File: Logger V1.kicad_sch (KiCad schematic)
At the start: 34 parts, among them J1 USB_C_Receptacle_USB2.0_16P, Q1 SS8050, Q2 SS8050, Q3 IRLML6402, SW1 B3U-1000P-B, SW2 B3U-1000P-B, U1 ESP32-WROOM-32E, U2 TLV76733DRVx, U3 LOG Interface, U4 oled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

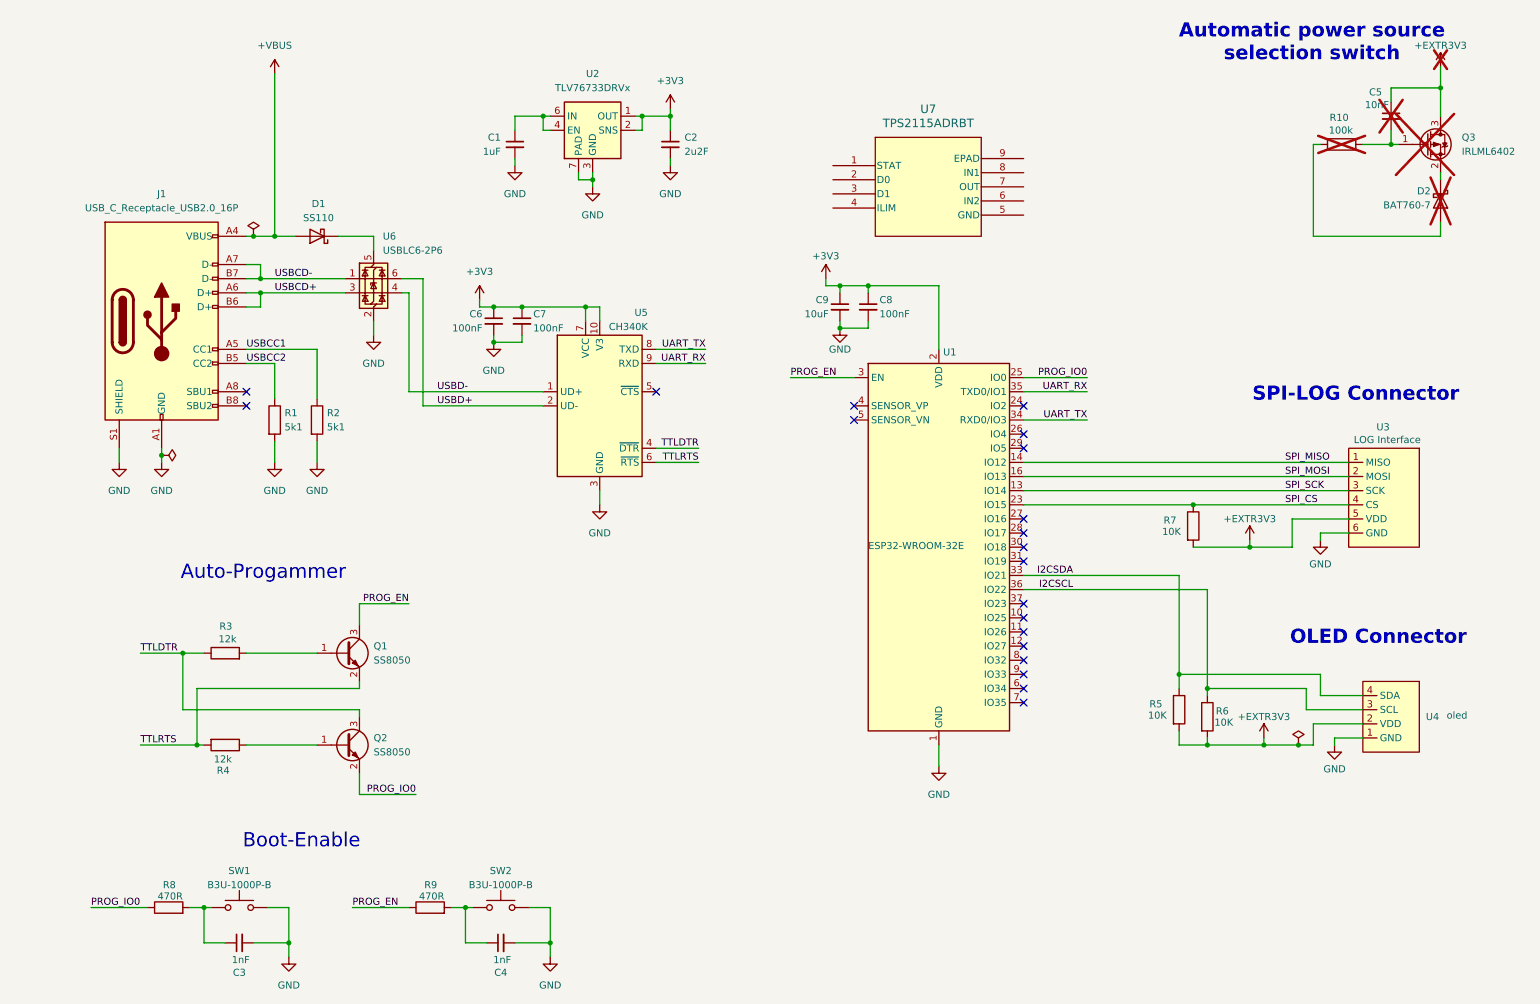
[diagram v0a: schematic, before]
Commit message: Schematic Finalized
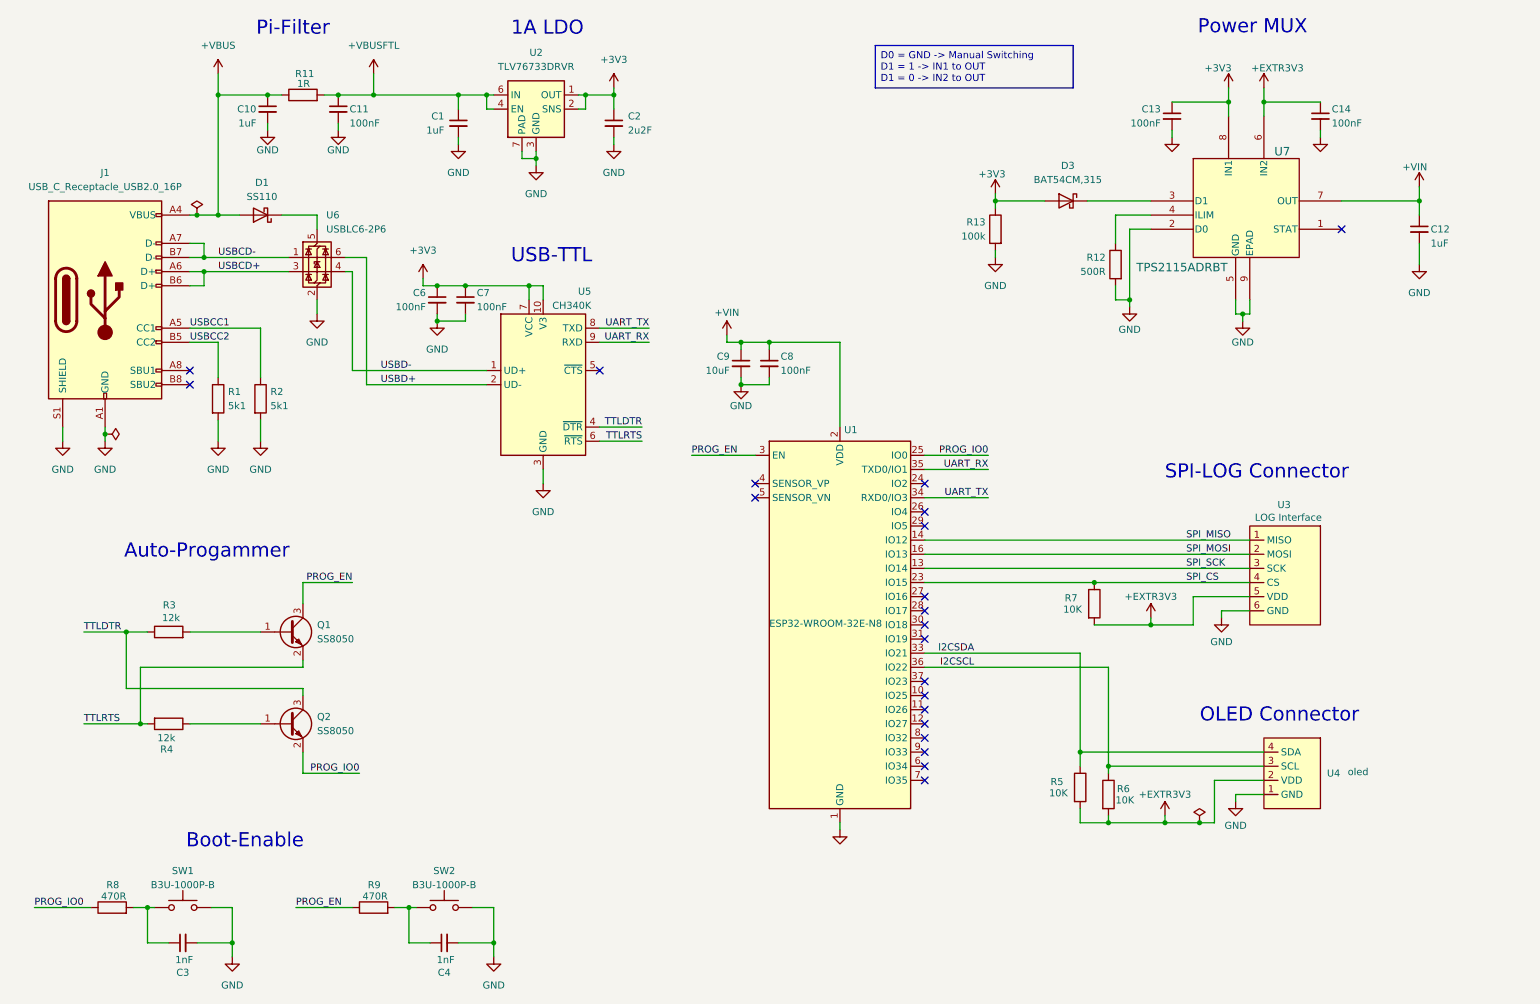
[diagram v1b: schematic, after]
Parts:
- removed C5: 10nF, Capacitor_SMD:C_0603_1608Metric_Pad1.08x0.95mm_HandSolder, symbol Device:C_Small
- removed D2: BAT760-7, Diode_SMD:D_SOD-323, symbol Device:D_Schottky
- removed Q3: IRLML6402, Package_TO_SOT_SMD:SOT-23, symbol Transistor_FET:IRLML6402
- removed R10: 100k, Resistor_SMD:R_0402_1005Metric_Pad0.72x0.64mm_HandSolder, symbol Device:R
- added C10, C12: 1uF, Capacitor_SMD:C_0603_1608Metric_Pad1.08x0.95mm_HandSolder, symbol Device:C_Small
- added C11, C13, C14: 100nF, Capacitor_SMD:C_0603_1608Metric_Pad1.08x0.95mm_HandSolder, symbol Device:C_Small
- added D3: BAT54CM,315, Package_DFN_QFN:Diodes_DFN1006-3, symbol Device:D_Schottky
- added R11: 1R, Resistor_SMD:R_0603_1608Metric_Pad0.98x0.95mm_HandSolder, symbol Device:R
- added R12: 500R, Resistor_SMD:R_0402_1005Metric_Pad0.72x0.64mm_HandSolder, symbol Device:R
- added R13: 100k, Resistor_SMD:R_0402_1005Metric_Pad0.72x0.64mm_HandSolder, symbol Device:R
- U1: value ESP32-WROOM-32E -> ESP32-WROOM-32E-N8; footprint RF_Module:ESP32-WROOM-32D -> RF_Module:ESP32-WROOM-32E; JLC.NUM (none) -> C701342; PRT.NUM (none) -> ESP32-WROOM-32E-N8
- U2: value TLV76733DRVx -> TLV76733DRVR; PRT.NUM (none) -> TLV76733DRVR
- U5: JLC.NUM (none) -> C968586; PRT.NUM (none) -> CH340K
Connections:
- net +3V3: now also U7.8 (IN1), C13.1, D3.2 (A), R13.1; no longer C8.1, C9.1, U1.2 (VDD)
- net +EXTR3V3: now also U7.6 (IN2), C14.1
- net +VBUS: now also C10.1, R11.1
- net GND: now also U7.2 (D0), U7.5 (GND), U7.9 (EPAD), C10.2, C11.2, C12.2, C13.2, C14.2, R12.2, R13.2
- net +VBUSFTL: now reaches C1.1, U2.4 (EN), U2.6 (IN)
- net +VBUSFTL: now also C11.1, R11.2
- net at U7.3 (D1): now also D3.1 (K)
- net at U7.4 (ILIM): now also R12.1
- net +VIN: now reaches U7.7 (OUT)
- net +VIN: now also C8.1, C9.1, U1.2 (VDD), C12.1
- no-connect marks 20 -> 21
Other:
- note added: "1A LDO"
- note added: "Pi-Filter"
- note added: "Power MUX"
- note added: "USB-TTL"
- note removed: "Automatic power source selection switch"
- moved on the sheet: C1, C2, C3, C4, C6, C7, C8, C9, D1, J1, Q1, Q2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

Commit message: PCB Rev 1.0
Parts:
- removed U4: oled, symbol logger:oled
- added TP1, TP2, TP3, TP4: TestPoint, TestPoint:TestPoint_Pad_1.0x1.0mm, symbol Connector:TestPoint
- C11, C13, C14, C3, C4, C6, C7, C8: footprint Capacitor_SMD:C_0603_1608Metric_Pad1.08x0.95mm_HandSolder -> Capacitor_SMD:C_0402_1005Metric_Pad0.74x0.62mm_HandSolder
- renumbered SW1 to BOOT1, SW2 to EN1
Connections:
- net +EXTR3V3: now also TP3.1; no longer R5.2, R6.2, R7.2
- net +VIN: now also R5.2, R6.2, R7.1
- net GND: now also TP4.1
- net I2CSCL: now also TP2.1
- net I2CSDA: now also TP1.1
- net SPI_CS: now also R7.2; no longer R7.1
- net UART_RX: now also U1.27 (IO16); no longer U1.35 (TXD0/IO1)
- net UART_TX: now also U1.28 (IO17); no longer U1.34 (RXD0/IO3)
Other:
- moved on the sheet: R5, R6, R7, U3

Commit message: ATIC Logger Rev1.0
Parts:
- removed C14: 100nF, Capacitor_SMD:C_0402_1005Metric_Pad0.74x0.62mm_HandSolder, symbol Device:C_Small
- added C5: 1uF, Capacitor_SMD:C_0603_1608Metric_Pad1.08x0.95mm_HandSolder, symbol Device:C_Small
- C1, C10: JLC.NUM C95843 -> C5673; PRT.NUM CL10B105KP8NNNC -> CL10A105KA8NNNC
- C11, C13, C6, C7, C8: JLC.NUM C1688 -> C100072; PRT.NUM CL10F104ZB8NNNC -> CL05A104KA5NNNC
- C12: value 1uF -> 100nF; footprint Capacitor_SMD:C_0603_1608Metric_Pad1.08x0.95mm_HandSolder -> Capacitor_SMD:C_0402_1005Metric_Pad0.74x0.62mm_HandSolder; JLC.NUM C95843 -> C100072; PRT.NUM CL10B105KP8NNNC -> CL05A104KA5NNNC
- C2: JLC.NUM C100082 -> C23630; PRT.NUM CL10B225KP8NNNC -> CL10A225KO8NNNC
- C3, C4: JLC.NUM C1588 -> C2649506; PRT.NUM CL10B102KB8NNNC -> C0402C102K5RACTU
- C9: JLC.NUM C19702 -> C96446; PRT.NUM CL10A106KP8NNNC -> CL10A106MA8NRNC
- TP1: value TestPoint -> SDA
- TP2: value TestPoint -> SCL
- TP3: value TestPoint -> EXTR3V3
- TP4: value TestPoint -> GND
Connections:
- net +3V3: now also C12.1; no longer C13.1
- net +EXTR3V3: now also C13.1
- net +VIN: now also C5.1; no longer C12.1
- net GND: now also C5.2
